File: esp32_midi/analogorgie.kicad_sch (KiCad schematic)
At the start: 15 parts, among them U5 BL1551

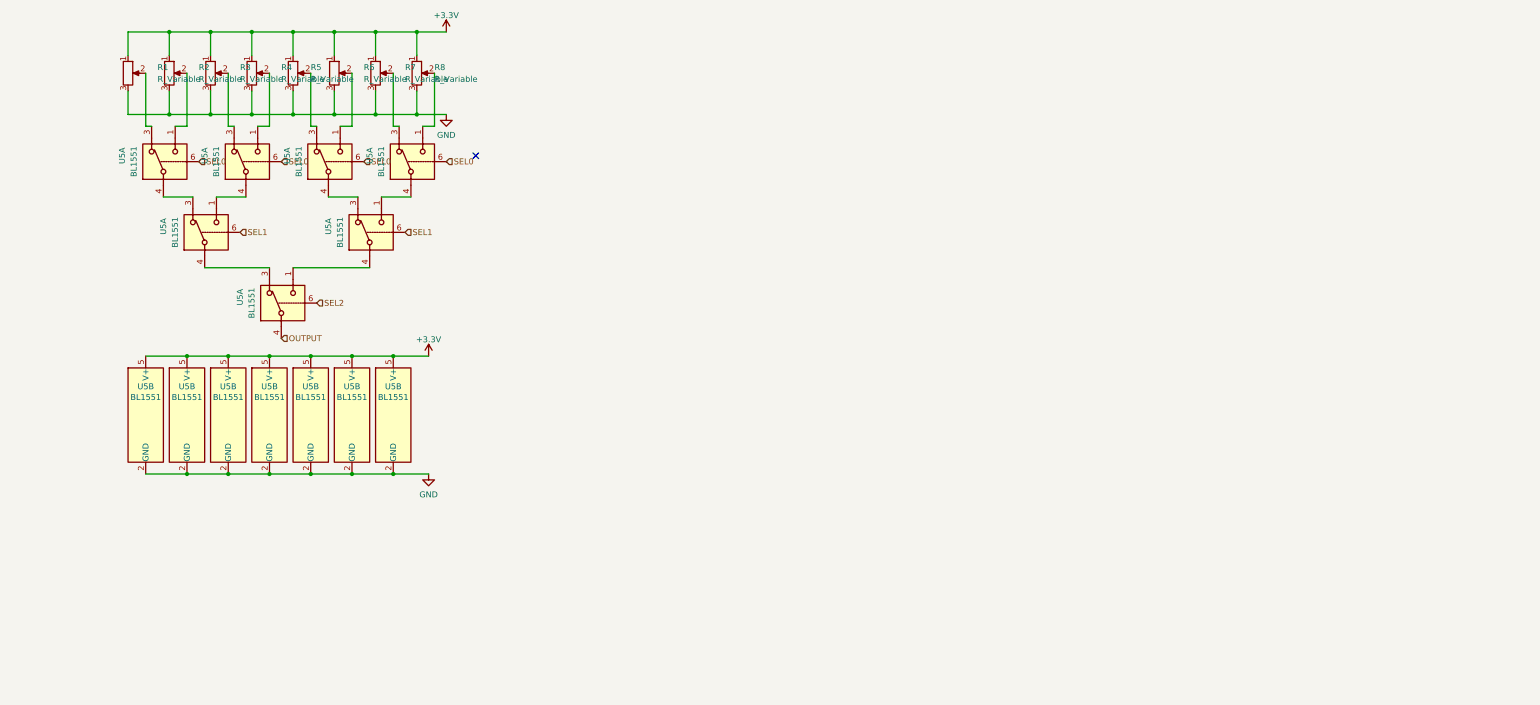
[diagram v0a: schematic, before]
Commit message: More footprints applied
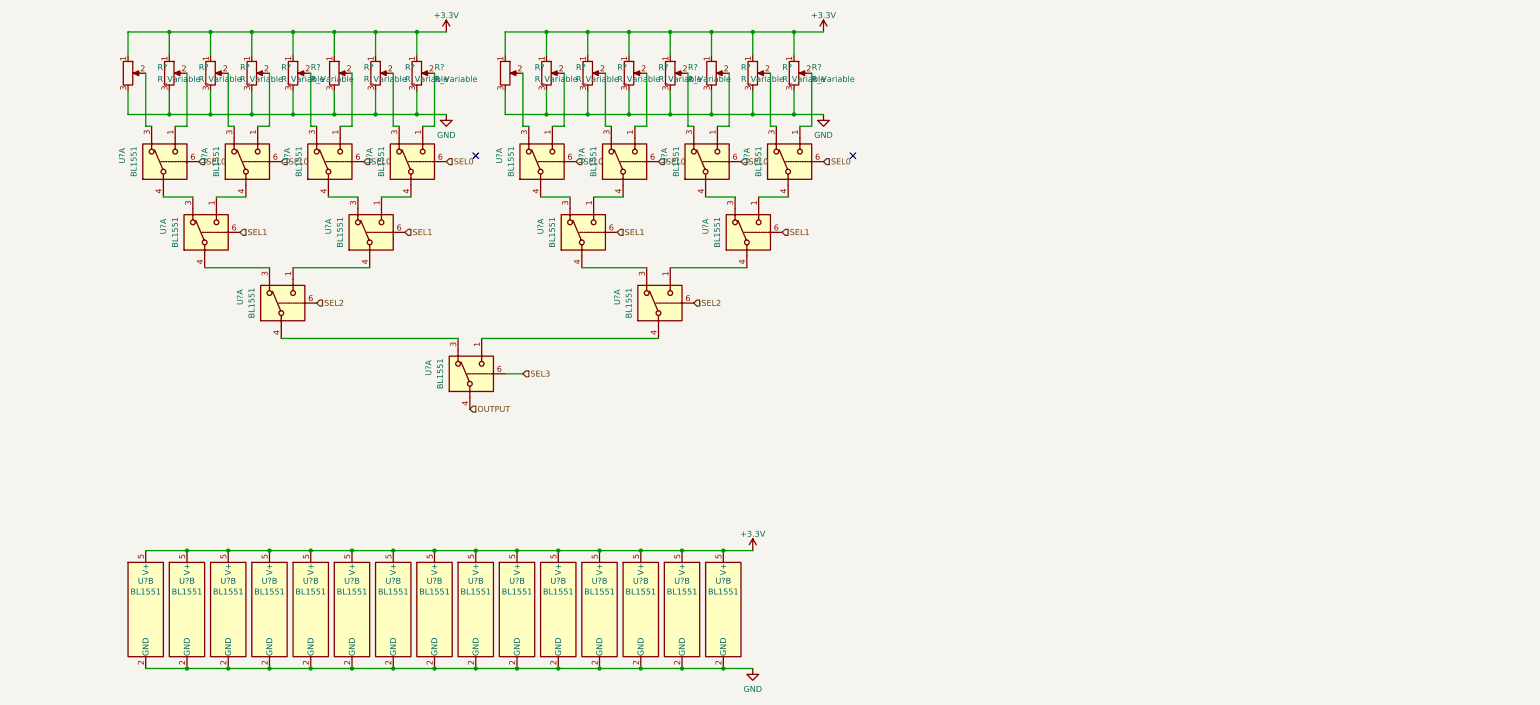
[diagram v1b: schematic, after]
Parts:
- added R? (x8): R_Variable, symbol Device:R_Potentiometer
- added U? (x16): BL1551, Package_TO_SOT_SMD:SOT-363_SC-70-6, symbol Analog_Switch:FSA3157L6X
- renumbered R1 to R?, R8 to R?, R3 to R?, R5 to R?, R4 to R?, R7 to R?, R2 to R?, R6 to R?, U5 to U?
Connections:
- net +3.3V: now also R?.1, R?.1, R?.1, R?.1, R?.1, R?.1, R?.1, R?.1, U?.5 (V+), U?.5 (V+), U?.5 (V+), U?.5 (V+), U?.5 (V+), U?.5 (V+), U?.5 (V+), U?.5 (V+)
- net GND: now also R?.3, R?.3, R?.3, R?.3, R?.3, R?.3, R?.3, R?.3, U?.2 (GND), U?.2 (GND), U?.2 (GND), U?.2 (GND), U?.2 (GND), U?.2 (GND), U?.2 (GND), U?.2 (GND)
- net OUTPUT: now also U?.4; no longer U?.4
- net SEL0: now also U?.6, U?.6, U?.6, U?.6
- net SEL1: now also U?.6, U?.6
- net SEL2: now also U?.6
- new net: U?.1, U?.4 (x4)
- new net: U?.3, U?.4 (x4)
- new net: R?.2, U?.1 (x4)
- new net: R?.2, U?.3 (x4)
- new net SEL3: U?.6
- no-connect marks 1 -> 2
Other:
- moved on the sheet: U?B

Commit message: Removed other bullshit projects
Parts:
- gave numbers to parts that had none: 15
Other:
- moved on the sheet: R?

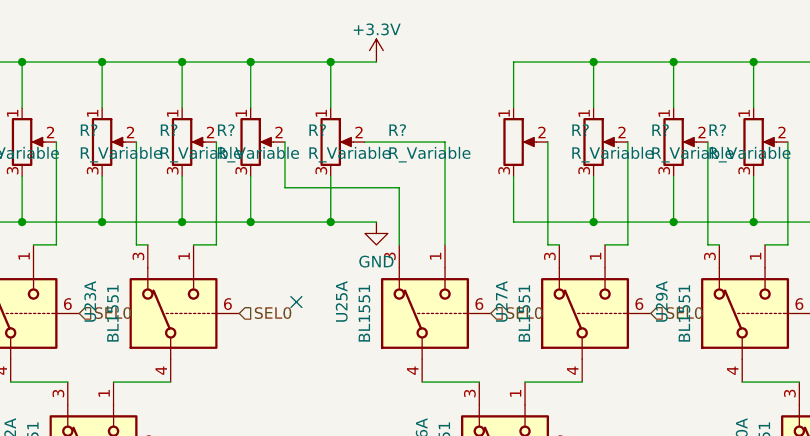
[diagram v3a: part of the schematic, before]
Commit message: Add 64buttons
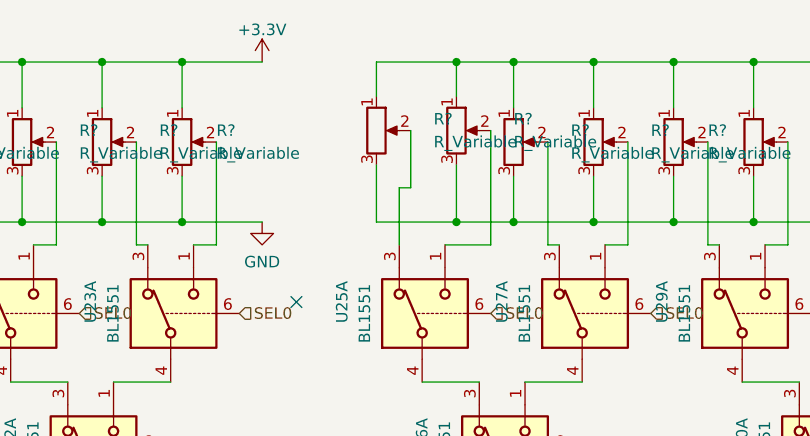
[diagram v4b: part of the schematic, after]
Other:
- moved on the sheet: R?
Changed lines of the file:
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@@
   (junction (at 63.5 49.53) (diameter 0) (color 0 0 0 0)
   )
+  (junction (at 129.54 49.53) (diameter 0) (color 0 0 0 0)
+  )
   (junction (at 93.98 168.91) (diameter 0) (color 0 0 0 0)
   )
@@
   (junction (at 85.09 168.91) (diameter 0) (color 0 0 0 0)
   )
+  (junction (at 99.06 31.75) (diameter 0) (color 0 0 0 0)
+  )
   (junction (at 67.31 143.51) (diameter 0) (color 0 0 0 0)
   )
-  (junction (at 106.68 49.53) (diameter 0) (color 0 0 0 0)
-  )
   (junction (at 171.45 49.53) (diameter 0) (color 0 0 0 0)
   )
@@
   (junction (at 49.53 143.51) (diameter 0) (color 0 0 0 0)
   )
+  (junction (at 99.06 49.53) (diameter 0) (color 0 0 0 0)
+  )
   (junction (at 138.43 168.91) (diameter 0) (color 0 0 0 0)
   )
-  (junction (at 106.68 31.75) (diameter 0) (color 0 0 0 0)
-  )
-  (junction (at 115.57 49.53) (diameter 0) (color 0 0 0 0)
+  (junction (at 135.89 31.75) (diameter 0) (color 0 0 0 0)
   )
   (junction (at 180.34 31.75) (diameter 0) (color 0 0 0 0)
@@
   (junction (at 72.39 49.53) (diameter 0) (color 0 0 0 0)
   )
-  (junction (at 99.06 31.75) (diameter 0) (color 0 0 0 0)
-  )
   (junction (at 76.2 143.51) (diameter 0) (color 0 0 0 0)
   )
@@
   (junction (at 81.28 31.75) (diameter 0) (color 0 0 0 0)
   )
-  (junction (at 99.06 49.53) (diameter 0) (color 0 0 0 0)
-  )
   (junction (at 72.39 31.75) (diameter 0) (color 0 0 0 0)
   )
@@
   (junction (at 58.42 143.51) (diameter 0) (color 0 0 0 0)
   )
-  (junction (at 115.57 31.75) (diameter 0) (color 0 0 0 0)
+  (junction (at 135.89 49.53) (diameter 0) (color 0 0 0 0)
+  )
+  (junction (at 129.54 31.75) (diameter 0) (color 0 0 0 0)
   )
   (junction (at 54.61 49.53) (diameter 0) (color 0 0 0 0)
@@
   (no_connect (at 193.04 58.42))
   (no_connect (at 111.76 58.42))
-  (wire (pts (xy 115.57 49.53) (xy 115.57 44.45))
-    (stroke (width 0) (type default))
-  )
-  (wire (pts (xy 110.49 45.72) (xy 123.19 45.72))
+  (wire (pts (xy 129.54 49.53) (xy 129.54 43.18))
+    (stroke (width 0) (type default))
+  )
+  (wire (pts (xy 124.46 45.72) (xy 123.19 45.72))
     (stroke (width 0) (type default))
   )
@@
     (stroke (width 0) (type default))
   )
-  (wire (pts (xy 106.68 49.53) (xy 115.57 49.53))
+  (wire (pts (xy 120.65 49.53) (xy 129.54 49.53))
+    (stroke (width 0) (type default))
+  )
+  (wire (pts (xy 133.35 52.07) (xy 128.27 52.07))
     (stroke (width 0) (type default))
   )
@@
     (stroke (width 0) (type default))
   )
+  (wire (pts (xy 129.54 49.53) (xy 135.89 49.53))
+    (stroke (width 0) (type default))
+  )
   (wire (pts (xy 153.67 49.53) (xy 162.56 49.53))
     (stroke (width 0) (type default))
@@
     (stroke (width 0) (type default))
   )
-  (wire (pts (xy 106.68 49.53) (xy 106.68 44.45))
+  (wire (pts (xy 120.65 49.53) (xy 120.65 43.18))
     (stroke (width 0) (type default))
   )
@@
     (stroke (width 0) (type default))
   )
-  (wire (pts (xy 115.57 49.53) (xy 120.65 49.53))
-    (stroke (width 0) (type default))
-  )
   (wire (pts (xy 180.34 49.53) (xy 180.34 44.45))
     (stroke (width 0) (type default))
@@
     (stroke (width 0) (type default))
   )
-  (wire (pts (xy 110.49 40.64) (xy 110.49 45.72))
+  (wire (pts (xy 124.46 39.37) (xy 124.46 45.72))
     (stroke (width 0) (type default))
   )
@@
     (stroke (width 0) (type default))
   )
-  (wire (pts (xy 115.57 31.75) (xy 115.57 36.83))
+  (wire (pts (xy 129.54 31.75) (xy 129.54 35.56))
     (stroke (width 0) (type default))
   )
@@
     (stroke (width 0) (type default))
   )
-  (wire (pts (xy 119.38 40.64) (xy 128.27 40.64))
-    (stroke (width 0) (type default))
-  )
   (wire (pts (xy 135.89 49.53) (xy 135.89 44.45))
     (stroke (width 0) (type default))
@@
     (stroke (width 0) (type default))
   )
-  (wire (pts (xy 128.27 40.64) (xy 128.27 52.07))
-    (stroke (width 0) (type default))
-  )
-  (wire (pts (xy 106.68 31.75) (xy 106.68 36.83))
+  (wire (pts (xy 133.35 39.37) (xy 133.35 52.07))
+    (stroke (width 0) (type default))
+  )
+  (wire (pts (xy 120.65 31.75) (xy 120.65 35.56))
     (stroke (width 0) (type default))
   )
@@
     (stroke (width 0) (type default))
   )
-  (wire (pts (xy 99.06 31.75) (xy 106.68 31.75))
-    (stroke (width 0) (type default))
-  )
   (wire (pts (xy 93.98 143.51) (xy 102.87 143.51))
     (stroke (width 0) (type default))
@@
     (stroke (width 0) (type default))
   )
-  (wire (pts (xy 115.57 31.75) (xy 120.65 31.75))
-    (stroke (width 0) (type default))
-  )
   (wire (pts (xy 175.26 52.07) (xy 176.53 52.07))
     (stroke (width 0) (type default))
@@
     (stroke (width 0) (type default))
   )
-  (wire (pts (xy 99.06 49.53) (xy 106.68 49.53))
-    (stroke (width 0) (type default))
-  )
   (wire (pts (xy 129.54 143.51) (xy 138.43 143.51))
     (stroke (width 0) (type default))
@@
     (stroke (width 0) (type default))
   )
+  (wire (pts (xy 107.95 31.75) (xy 99.06 31.75))
+    (stroke (width 0) (type default))
+  )
   (wire (pts (xy 58.42 143.51) (xy 67.31 143.51))
     (stroke (width 0) (type default))
@@
     (stroke (width 0) (type default))
   )
+  (wire (pts (xy 129.54 31.75) (xy 135.89 31.75))
+    (stroke (width 0) (type default))
+  )
   (wire (pts (xy 144.78 49.53) (xy 144.78 44.45))
     (stroke (width 0) (type default))
   )
+  (wire (pts (xy 99.06 49.53) (xy 107.95 49.53))
+    (stroke (width 0) (type default))
+  )
   (wire (pts (xy 54.61 31.75) (xy 63.5 31.75))
     (stroke (width 0) (type default))
@@
     (stroke (width 0) (type default))
   )
-  (wire (pts (xy 106.68 31.75) (xy 115.57 31.75))
+  (wire (pts (xy 120.65 31.75) (xy 129.54 31.75))
     (stroke (width 0) (type default))
   )
@@
     )
   )
-  (symbol (lib_id "power:+3.3V") (at 120.65 31.75 0) (unit 1)
+  (symbol (lib_id "power:+3.3V") (at 107.95 31.75 0) (unit 1)
     (in_bom yes) (on_board yes) (dnp no) (fields_autoplaced)
-    (property "Reference" "#PWR?" (at 120.65 35.56 0)
-      (effects (font (size 1.27 1.27)) hide)
-    )
-    (property "Value" "+3.3V" (at 120.65 28.1742 0)
-      (effects (font (size 1.27 1.27)))
-    )
-    (property "Footprint" "" (at 120.65 31.75 0)
-      (effects (font (size 1.27 1.27)) hide)
-    )
-    (property "Datasheet" "" (at 120.65 31.75 0)
+    (property "Reference" "#PWR?" (at 107.95 35.56 0)
+      (effects (font (size 1.27 1.27)) hide)
+    )
+    (property "Value" "+3.3V" (at 107.95 28.1742 0)
+      (effects (font (size 1.27 1.27)))
+    )
+    (property "Footprint" "" (at 107.95 31.75 0)
+      (effects (font (size 1.27 1.27)) hide)
+    )
+    (property "Datasheet" "" (at 107.95 31.75 0)
       (effects (font (size 1.27 1.27)) hide)
     )
@@
     )
   )
-  (symbol (lib_id "Device:R_Potentiometer") (at 106.68 40.64 0) (unit 1)
-    (in_bom yes) (on_board yes) (dnp no)
-    (property "Reference" "R?" (at 113.03 39.37 0)
-      (effects (font (size 1.27 1.27)) (justify left))
-    )
-    (property "Value" "R_Variable" (at 113.03 41.91 0)
-      (effects (font (size 1.27 1.27)) (justify left))
-    )
-    (property "Footprint" "" (at 106.68 40.64 0)
-      (effects (font (size 1.27 1.27)) hide)
-    )
-    (property "Datasheet" "~" (at 106.68 40.64 0)
+  (symbol (lib_id "Device:R_Potentiometer") (at 120.65 39.37 0) (unit 1)
+    (in_bom yes) (on_board yes) (dnp no)
+    (property "Reference" "R?" (at 127 38.1 0)
+      (effects (font (size 1.27 1.27)) (justify left))
+    )
+    (property "Value" "R_Variable" (at 127 40.64 0)
+      (effects (font (size 1.27 1.27)) (justify left))
+    )
+    (property "Footprint" "" (at 120.65 39.37 0)
+      (effects (font (size 1.27 1.27)) hide)
+    )
+    (property "Datasheet" "~" (at 120.65 39.37 0)
       (effects (font (size 1.27 1.27)) hide)
     )
@@
     )
   )
-  (symbol (lib_id "Device:R_Potentiometer") (at 115.57 40.64 0) (unit 1)
-    (in_bom yes) (on_board yes) (dnp no)
-    (property "Reference" "R?" (at 121.92 39.37 0)
-      (effects (font (size 1.27 1.27)) (justify left))
-    )
-    (property "Value" "R_Variable" (at 121.92 41.91 0)
-      (effects (font (size 1.27 1.27)) (justify left))
-    )
-    (property "Footprint" "" (at 115.57 40.64 0)
-      (effects (font (size 1.27 1.27)) hide)
-    )
-    (property "Datasheet" "~" (at 115.57 40.64 0)
+  (symbol (lib_id "Device:R_Potentiometer") (at 129.54 39.37 0) (unit 1)
+    (in_bom yes) (on_board yes) (dnp no)
+    (property "Reference" "R?" (at 135.89 38.1 0)
+      (effects (font (size 1.27 1.27)) (justify left))
+    )
+    (property "Value" "R_Variable" (at 135.89 40.64 0)
+      (effects (font (size 1.27 1.27)) (justify left))
+    )
+    (property "Footprint" "" (at 129.54 39.37 0)
+      (effects (font (size 1.27 1.27)) hide)
+    )
+    (property "Datasheet" "~" (at 129.54 39.37 0)
       (effects (font (size 1.27 1.27)) hide)
     )
@@
     )
   )
-  (symbol (lib_id "power:GND") (at 120.65 49.53 0) (unit 1)
+  (symbol (lib_id "power:GND") (at 107.95 49.53 0) (unit 1)
     (in_bom yes) (on_board yes) (dnp no) (fields_autoplaced)
-    (property "Reference" "#PWR?" (at 120.65 55.88 0)
-      (effects (font (size 1.27 1.27)) hide)
-    )
-    (property "Value" "GND" (at 120.65 53.9734 0)
-      (effects (font (size 1.27 1.27)))
-    )
-    (property "Footprint" "" (at 120.65 49.53 0)
-      (effects (font (size 1.27 1.27)) hide)
-    )
-    (property "Datasheet" "" (at 120.65 49.53 0)
-      (effects (font (size 1.27 1.27)) hide)
-    )
+    (property "Reference" "#PWR?" (at 107.95 55.88 0)
+      (effects (font (size 1.27 1.27)) hide)
+    )
+    (property "Value" "GND" (at 107.95 53.9734 0)
+      (effects (font (size 1.27 1.27)))
+    )
+    (property "Footprint" "" (at 107.95 49.53 0)
+      (effects (font (size 1.27 1.27)) hide)
+    )
+    (property "Datasheet" "" (at 107.95 49.53 0)
+      (effects (font (size 1.27 1.27)) hide)
+    )

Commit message: Updated pcb
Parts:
- added R? (x16): R_Variable, symbol Device:R_Potentiometer
- added U21, U22, U23, U24, U25, U26, U27, U28, U29, U30, U31, U32, U33, U34, U35: BL1551, Package_TO_SOT_SMD:SOT-363_SC-70-6, symbol Analog_Switch:FSA3157L6X
- renumbered U21 to U10, U22 to U11, U23 to U12, U24 to U13, U25 to U14, U26 to U15, U27 to U16, U28 to U17, U29 to U18, U30 to U19, U31 to U20, U17 to U6, U18 to U7, U19 to U8, U20 to U9
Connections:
- net +3.3V: now also R?.1, R?.1, R?.1, R?.1, R?.1, R?.1, R?.1, R?.1, R?.1, R?.1, R?.1, R?.1, R?.1, R?.1, R?.1, R?.1, U21.5 (V+), U22.5 (V+), U23.5 (V+), U24.5 (V+), U25.5 (V+), U26.5 (V+), U27.5 (V+), U28.5 (V+), U29.5 (V+), U30.5 (V+), U31.5 (V+), U32.5 (V+), U33.5 (V+), U34.5 (V+), U35.5 (V+)
- net GND: now also R?.3, R?.3, R?.3, R?.3, R?.3, R?.3, R?.3, R?.3, R?.3, R?.3, R?.3, R?.3, R?.3, R?.3, R?.3, R?.3, U21.2 (GND), U22.2 (GND), U23.2 (GND), U24.2 (GND), U25.2 (GND), U26.2 (GND), U27.2 (GND), U28.2 (GND), U29.2 (GND), U30.2 (GND), U31.2 (GND), U32.2 (GND), U33.2 (GND), U34.2 (GND), U35.2 (GND)
- net SEL0: now also U21.6, U23.6, U25.6, U27.6, U29.6, U31.6, U33.6, U35.6
- net SEL1: now also U22.6, U26.6, U30.6, U34.6
- net SEL2: now also U24.6, U32.6
- net SEL3: now also U28.6
- net OUTPUT renamed OUTPUT0
- new net: R?.2, U29.1
- new net: R?.2, U35.3
- new net: R?.2, U21.1
- new net: R?.2, U27.1
- new net: U34.1, U35.4
- new net: U33.4, U34.3
- new net: U32.1, U34.4
- new net: R?.2, U31.1
- new net: R?.2, U35.1
- new net: R?.2, U33.1
- new net: R?.2, U33.3
- new net: R?.2, U27.3
- new net: U22.1, U23.4
- new net: U21.4, U22.3
- new net: U22.4, U24.3
- new net: U26.1, U27.4
- new net: U30.4, U32.3
- new net: U28.1, U32.4
- new net: U30.1, U31.4
- new net: U29.4, U30.3
- new net: R?.2, U25.1
- new net: R?.2, U29.3
- new net: R?.2, U25.3
- new net: R?.2, U31.3
- new net: U25.4, U26.3
- new net: U24.1, U26.4
- new net: R?.2, U23.1
- new net: R?.2, U23.3
- new net: R?.2, U21.3
- new net: U24.4, U28.3
- new net OUTPUT1: U28.4
- no-connect marks 2 -> 4
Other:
- moved on the sheet: R?, U10A, U10B, U11A, U11B, U12A, U12B, U13A, U13B, U14A, U14B, U15A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

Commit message: Add ordentliche-teile
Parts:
- added U108, U114: BL1551, Package_TO_SOT_SMD:SOT-363_SC-70-6, symbol Analog_Switch:FSA3157L6X
- R? (x8): footprint (none) -> ordentliche-teile:scheißfader
- R? (x24): footprint (none) -> Potentiometer_THT:Potentiometer_Alps_RK09L_Single_Vertical
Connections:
- net +3.3V: now also U108.5 (V+)
- net GND: now also U108.2 (GND)
- net OUTPUT0: no longer names the net of U13.4
- net OUTPUT0: now also U114.3
- net OUTPUT1: no longer names the net of U28.4
- net OUTPUT1: now also U114.1
- new net OUTPUT: U114.4
- new net SEL4: U114.6
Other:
- moved on the sheet: U10B, U11B, U12B, U13B, U14B, U15B, U16B, U17B, U18B, U19B, U20B, U21B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
